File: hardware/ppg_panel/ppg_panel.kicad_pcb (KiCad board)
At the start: 2 copper layers, 70 x 110 mm, 68 parts

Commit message: Convert PPG passives to SMD and refresh compact V-cut panel
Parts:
- OPT_C1, OPT_C2: footprint OPT_PPG:Bypass_100n_P2.5mm -> OPT_PPG:C0805_Hand
- TX_R4, TX_R9: footprint TX_TX:R -> TX_TX:RSense
- moved TX_R1 3.81 mm to (62.8, 132.0)
- moved TX_R2 3.81 mm to (62.8, 136.0)
- moved TX_R3 3.81 mm to (73.0, 138.3)
- moved TX_R4 3.81 mm to (65.8, 151.0)
- moved TX_R6 3.81 mm to (99.8, 132.0)
- moved TX_R7 3.81 mm to (99.8, 136.0)
- moved TX_R8 3.81 mm to (99.8, 140.0)
- moved TX_R9 3.81 mm to (101.8, 151.0)
- moved TX_H3 2.00 mm to (54.0, 154.0)
- moved TX_H4 2.00 mm to (116.0, 154.0)
- moved OPT_C1 1.25 mm to (63.2, 57.0)
- moved OPT_C2 1.25 mm to (101.7, 57.0)
- moved TX_C2 1.25 mm to (77.0, 144.2)
- moved TX_C4 1.25 mm to (93.0, 144.2)
- moved TX_C5 1.25 mm to (90.1, 131.0)
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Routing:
- net TX/GND: track 0.00 -> 11.6 mm, vias 0 -> 6
- net TX/CMD_RED: track 29.6 -> 35.2 mm, vias 0 -> 1
- net TX/CMD_IR: track 21.7 -> 27.3 mm, vias 0 -> 2
- net TX/AMP_RED: track 14.3 -> 17.3 mm
- net TX/AMP_IR: track 21.2 -> 24.2 mm, vias 0 -> 1
- net TX/DAC_IR: track 41.5 -> 44.3 mm, vias 0 -> 1
- net TX/DAC_RED: track 46.7 -> 49.5 mm, vias 0 -> 1
- net TX/BASE_RED: track 10.1 -> 12.9 mm
- net TX/BASE_IR: track 6.34 -> 9.15 mm
- net TX/SENSE_RED: track 35.8 -> 38.3 mm, vias 0 -> 2
- net TX/SENSE_IR: track 46.2 -> 48.6 mm, vias 0 -> 2
- net TX/5V: track 68.4 -> 69.8 mm, vias 0 -> 1
- net OPT/3V3_RED: track 38.1 -> 38.3 mm, vias 0 -> 1
- net OPT/3V3_IR: track 43.8 -> 44.0 mm, vias 0 -> 1
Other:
- board size 70 x 110 mm -> 70 x 108 mm
- board text added: "PPG RX v1.4"
- board text added: "PPG TX v1.8"
- board text removed: "5V GND"
- board text removed: "DAC: 3.3V ONLY"
- board text removed: "IR A+ K-"
- board text removed: "J2 PI: SCL SDA 3V3 GND"
- board text removed: "PPG RX v1.3"
- board text removed: "PPG TX v1.7"
- board text removed: "RED A+ K-"

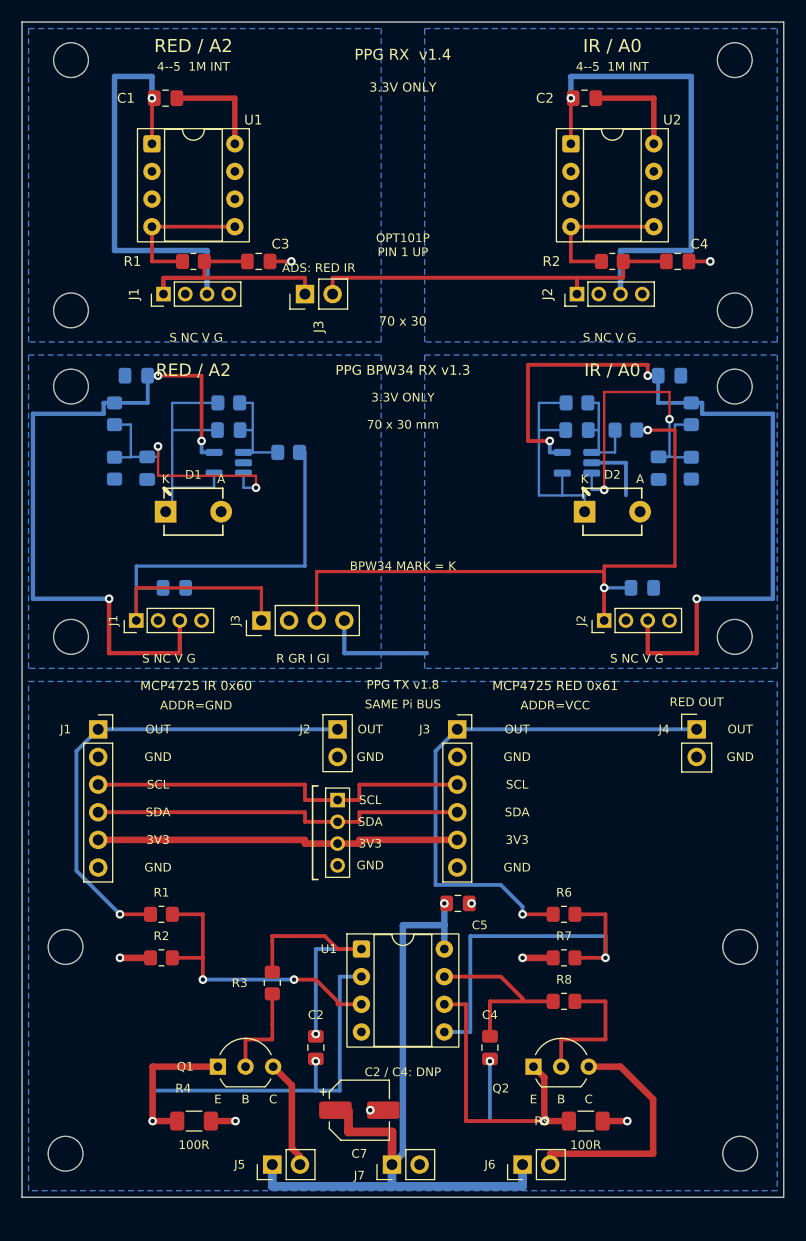
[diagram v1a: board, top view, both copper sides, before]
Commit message: Shrink PPG receivers to 70x20 and driver to 70x40; refresh V-cut release
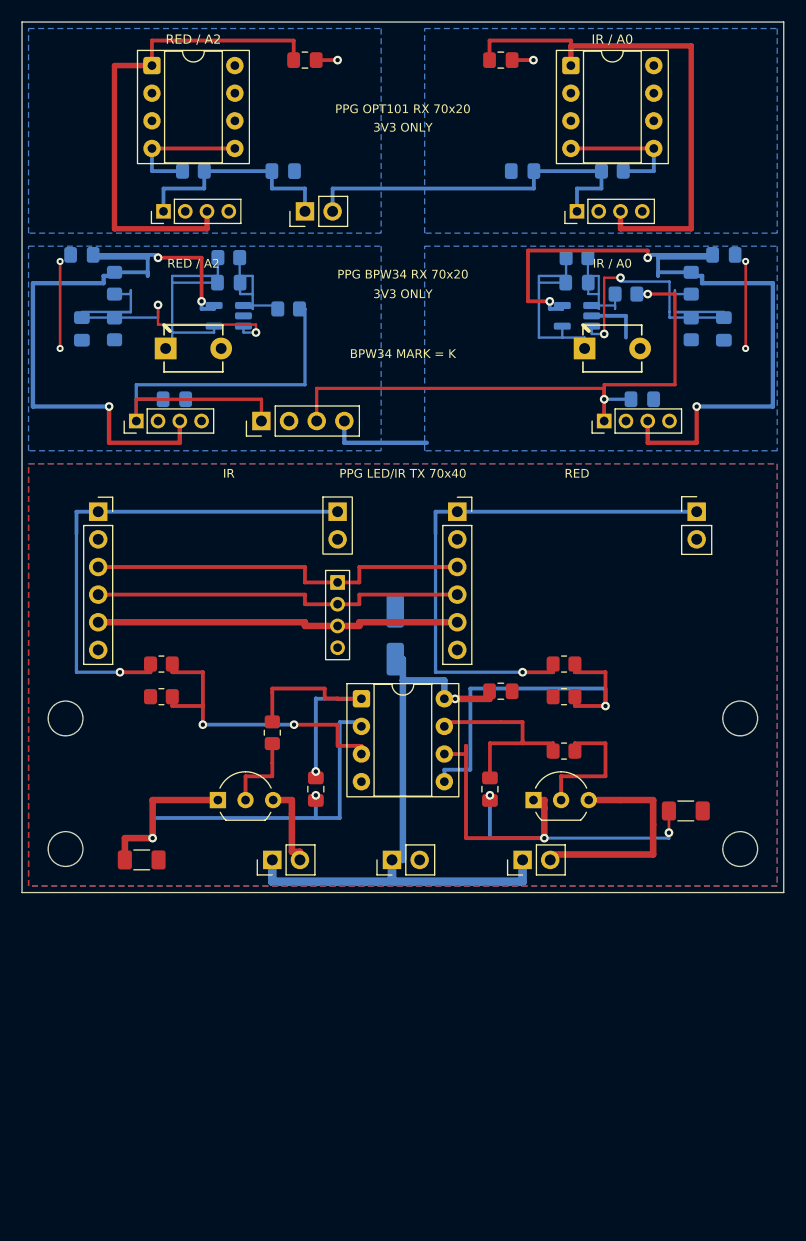
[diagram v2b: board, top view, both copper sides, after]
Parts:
- removed BPW_H1, BPW_H2, BPW_H3, BPW_H4: M3 / 3.2mm NPTH, BPW_PPG:MountingHole_M3
- removed OPT_H1, OPT_H2, OPT_H3, OPT_H4: M3 / 3.2mm NPTH, OPT_PPG:MountingHole_M3
- OPT_C3, OPT_C4, OPT_R1, OPT_R2, TX_C7: moved to B.Cu
- moved TX_C7 43.8 mm to (84.3, 106.3), turned to 90 degrees
- moved TX_R9 29.9 mm to (111.0, 122.5)
- moved TX_H3 28.0 mm to (54.0, 126.0)
- moved TX_H4 28.0 mm to (116.0, 126.0)
- moved TX_J5 28.0 mm to (73.0, 127.0)
- moved TX_J6 28.0 mm to (96.0, 127.0)
- moved TX_J7 28.0 mm to (84.0, 127.0)
- moved TX_Q1 24.5 mm to (68.0, 121.5)
- moved TX_Q2 24.5 mm to (97.0, 121.5)
- moved TX_R4 24.5 mm to (61.0, 127.0)
- moved TX_R2 24.0 mm to (62.8, 112.0)
- moved TX_R7 24.0 mm to (99.8, 112.0)
- moved TX_C2 23.8 mm to (77.0, 120.5)
- moved TX_C4 23.8 mm to (93.0, 120.5)
- moved TX_R1 23.0 mm to (62.8, 109.0)
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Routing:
- net TX/GND: track 11.6 -> 0.00 mm, vias 6 -> 0
- net TX/5V: track 69.8 -> 59.5 mm
- net OPT/GND_RED: track 11.5 -> 1.96 mm
- net OPT/GND_IR: track 11.5 -> 1.96 mm
- net BPW/OUT_IR: track 65.4 -> 56.5 mm
- net BPW/GND_RED: track 0.00 -> 8.00 mm, vias 0 -> 2
- net TX/SENSE_RED: track 38.3 -> 46.3 mm, vias 2 -> 3
- net BPW/VREF_RED: track 24.8 -> 32.3 mm
- net OPT/3V3_RED: track 38.3 -> 45.7 mm, vias 1 -> 0
- net BPW/OUT_RED: track 51.4 -> 44.3 mm
- net OPT/OUT_RED: track 26.7 -> 20.4 mm
- net BPW/GND_IR: track 16.7 -> 22.7 mm, vias 0 -> 2
- net OPT/3V3_IR: track 44.0 -> 49.3 mm, vias 1 -> 0
- net BPW/SUM_RED: track 25.0 -> 22.3 mm
- net BPW/SUM_IR: track 21.2 -> 18.6 mm
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- added copper zone on F.Cu, net TX/GND
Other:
- board size 70 x 108 mm -> 70 x 80 mm
- board text added: "3V3 ONLY"
- board text added: "IR"
- board text added: "IR-"
- board text added: "PPG BPW34 RX 70x20"
- board text added: "PPG LED/IR TX 70x40"
- board text added: "PPG OPT101 RX 70x20"
- board text added: "RED"
- board text added: "RED-"
- board text added: "S"
- board text removed: "100R"
- board text removed: "3.3V ONLY"
- board text removed: "4--5 1M INT"
- board text removed: "70 x 30"
- board text removed: "70 x 30 mm"
- board text removed: "A+"
- board text removed: "ADDR=GND"
- board text removed: "ADDR=VCC"
- board text removed: "ADS: RED IR"
- board text removed: "C1"
- board text removed: "C2"
- board text removed: "C2 / C4: DNP"
- board text removed: "C3"
- board text removed: "C4"
- board text removed: "C5"
- board text removed: "C6"
- board text removed: "C7"
- board text removed: "C8"
- board text removed: "D1"
- board text removed: "D1 RED"
- board text removed: "D2"
- board text removed: "D2 IR"
- board text removed: "GR/GI=CHANNEL GND"
- board text removed: "IR_OUT"
- board text removed: "J1"
- board text removed: "J1 A2 RED"
- board text removed: "J1 IR DAC"
- board text removed: "J2"
- board text removed: "J2 A0 IR"
- board text removed: "J2 PI"
- board text removed: "J3"
- board text removed: "J3 ADS"
- board text removed: "J3 RED DAC"
- board text removed: "J4"
- board text removed: "J4 RED OUT"
- board text removed: "J5"
- board text removed: "J5 IR LED"
- board text removed: "J6"
- board text removed: "J6 RED LED"
- board text removed: "J7"
- board text removed: "J7 POWER"
- board text removed: "K-"
- board text removed: "MCP4725 IR 0x60"
- board text removed: "MCP4725 RED 0x61"
- board text removed: "N"
- board text removed: "OPT101P PIN 1 UP"
- board text removed: "PPG BPW34 RX v1.3"
- board text removed: "PPG RX v1.4"
- board text removed: "PPG TX v1.8"
- board text removed: "Q1"
- board text removed: "Q1 IR E-B-C"
- board text removed: "Q2"
- board text removed: "Q2 RED E-B-C"
- board text removed: "R GR I GI"
- board text removed: "R1"
- board text removed: "R2"
- board text removed: "R3"
- board text removed: "R4"
- board text removed: "R5"
- board text removed: "R6"
- board text removed: "R7"
- board text removed: "R8"
- board text removed: "R9"
- board text removed: "R=OUT_RED I=OUT_IR"
- board text removed: "RED OUT"
- board text removed: "RED_OUT"
- board text removed: "S NC V G"
- board text removed: "SAME Pi BUS"
- board text removed: "U1"
- board text removed: "U1 LM358"
- board text removed: "U1 RED OPT101"
- board text removed: "U2"
- board text removed: "U2 IR OPT101"
- board text removed: "V=3V3 GR/GI=GND"
- board text removed: "V=3V3 N=NC"

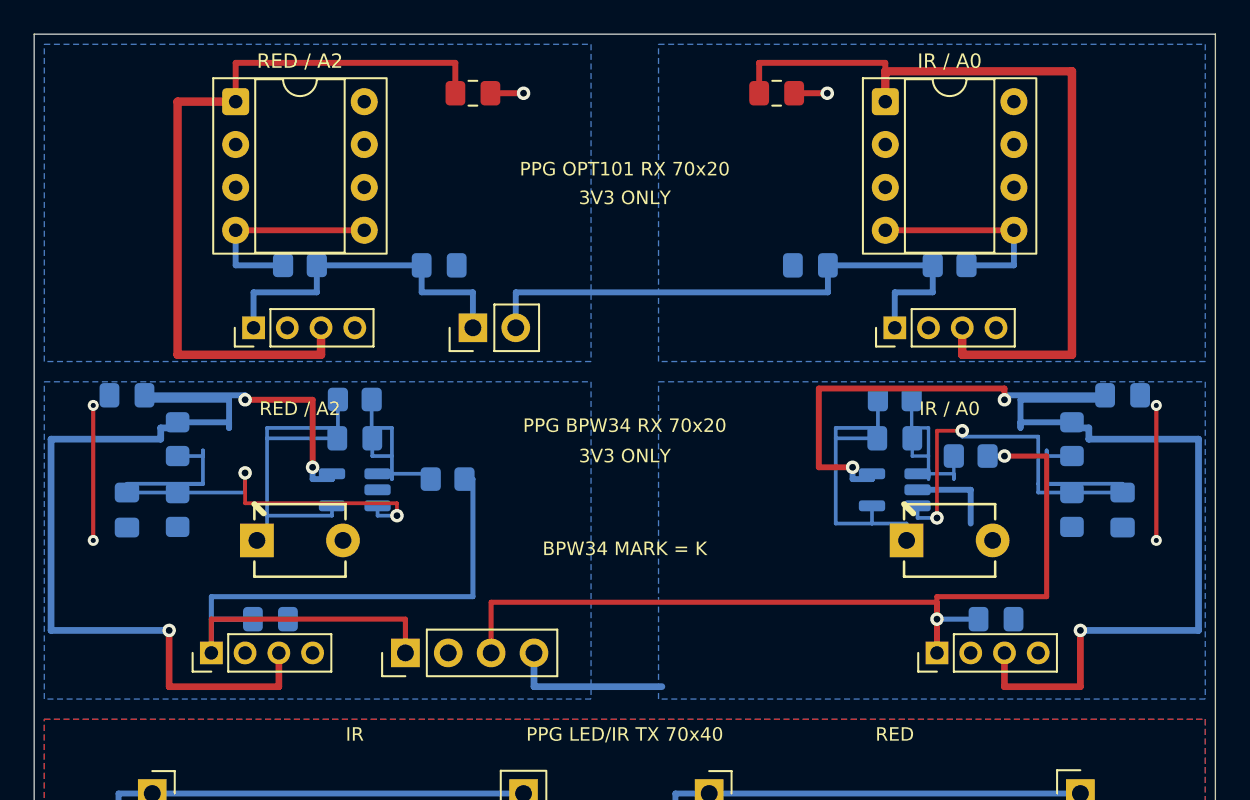
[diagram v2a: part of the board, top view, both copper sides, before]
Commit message: Increase V-score copper and component margins; reposition receiver circuits
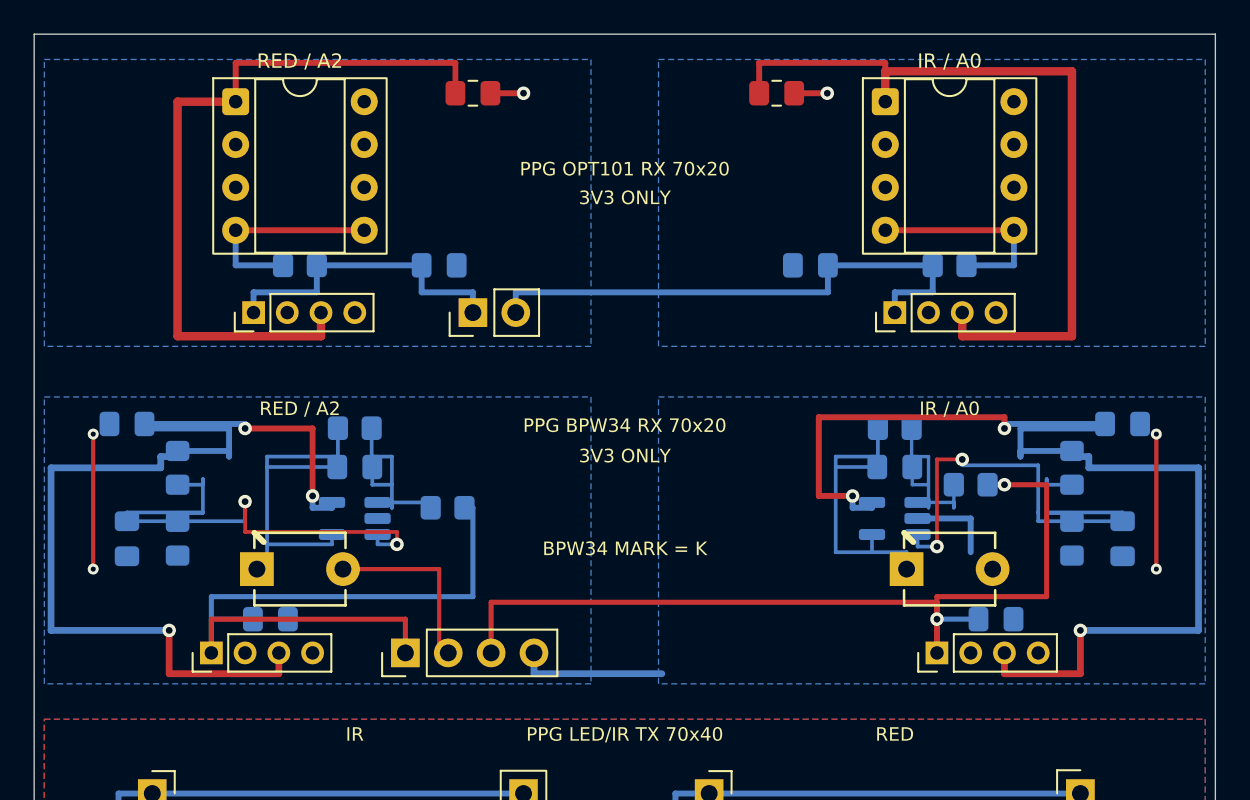
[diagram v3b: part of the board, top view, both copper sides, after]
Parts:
- moved BPW_C1 1.70 mm to (69.0, 75.7)
- moved BPW_C2 1.70 mm to (101.0, 75.7)
- moved BPW_C3 1.70 mm to (55.5, 79.9)
- moved BPW_C4 1.70 mm to (114.5, 79.9)
- moved BPW_D1 1.70 mm to (65.8, 81.7)
- moved BPW_D2 1.70 mm to (104.2, 81.7)
- moved BPW_R3 1.70 mm to (74.5, 78.1)
- moved BPW_R4 1.70 mm to (105.5, 76.7)
- moved BPW_R5 1.70 mm to (58.5, 75.7)
- moved BPW_R6 1.70 mm to (111.5, 75.7)
- moved BPW_R7 1.70 mm to (58.5, 79.9)
- moved BPW_R8 1.70 mm to (111.5, 79.9)
- moved BPW_U1 1.70 mm to (69.0, 78.7)
- moved BPW_U2 1.70 mm to (101.0, 78.7)
- moved BPW_C5 1.70 mm to (55.5, 73.1)
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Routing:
- net BPW/GND_RED: track 8.00 -> 19.2 mm
- net BPW/3V3_IR: track 73.7 -> 70.5 mm
- net BPW/3V3_RED: track 65.4 -> 62.2 mm
- net OPT/OUT_RED: track 20.4 -> 18.6 mm
- net OPT/OUT_IR: track 34.4 -> 32.6 mm
- net BPW/OUT_RED: track 44.3 -> 42.6 mm
- net BPW/OUT_IR: track 56.5 -> 54.8 mm
- net OPT/3V3_RED: track 45.7 -> 44.4 mm
- net OPT/3V3_IR: track 49.3 -> 48.0 mm
- net BPW/GND_IR: track 22.7 -> 22.0 mm

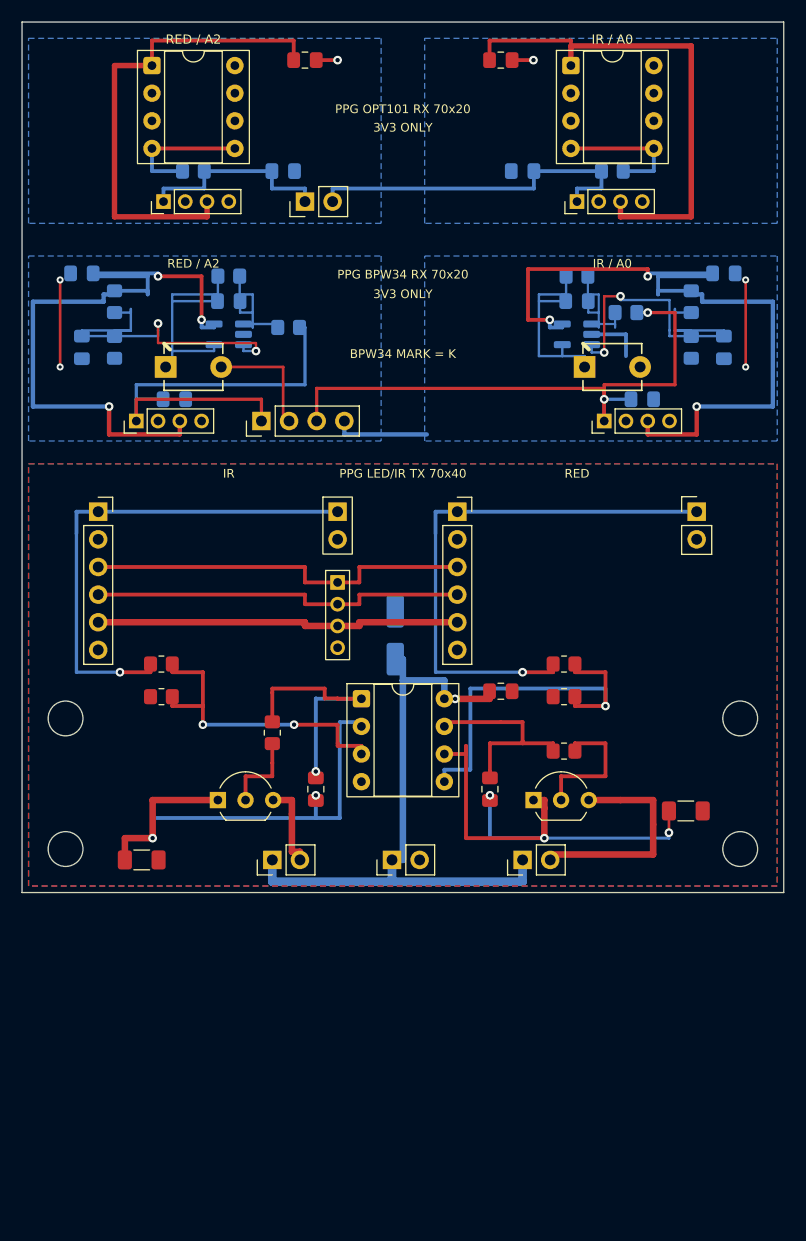
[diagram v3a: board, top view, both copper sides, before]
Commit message: Chamfer PPG board routing to 45 degrees and verify V-score fabrication release
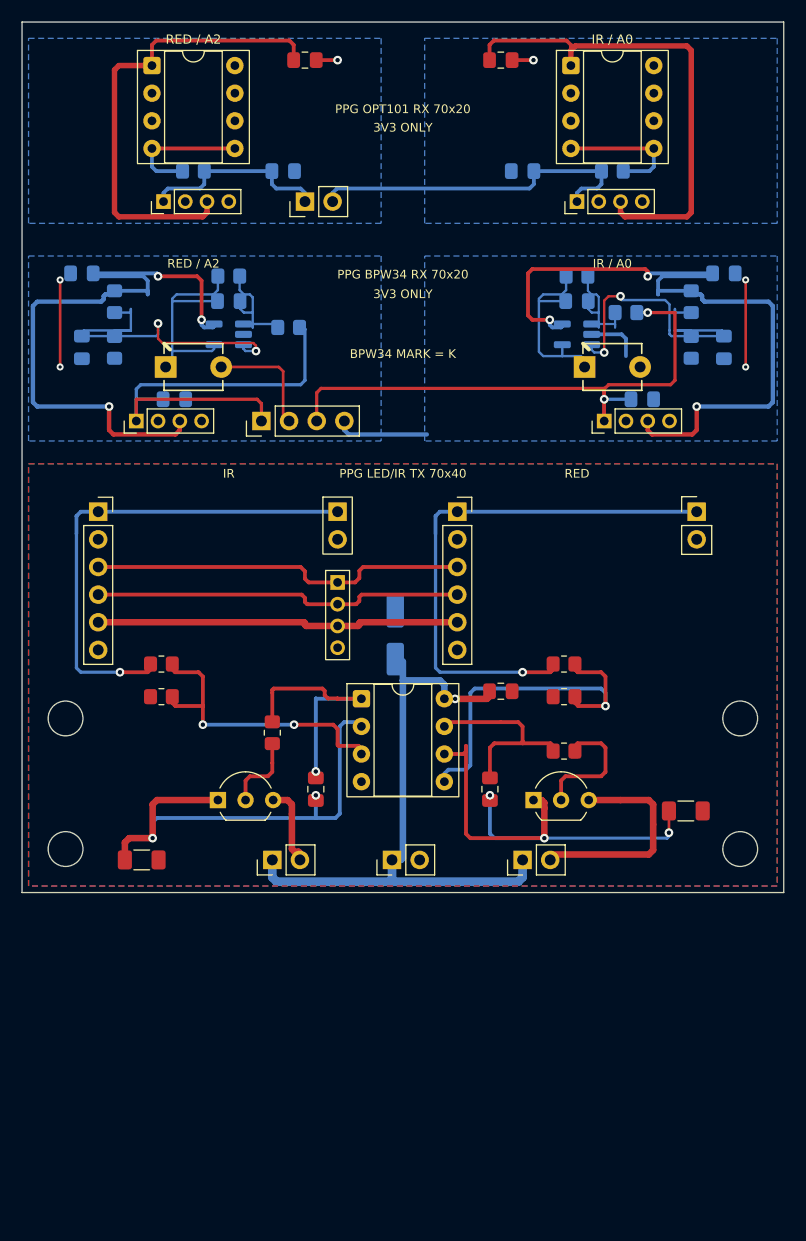
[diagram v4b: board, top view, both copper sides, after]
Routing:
- net BPW/3V3_IR: track 70.5 -> 68.1 mm
- net BPW/3V3_RED: track 62.2 -> 60.2 mm
- net TX/CMD_RED: track 35.3 -> 33.8 mm
- net OPT/3V3_IR: track 48.0 -> 46.6 mm
- net OPT/3V3_RED: track 44.4 -> 43.2 mm
- net TX/SENSE_IR: track 46.5 -> 45.3 mm
- net TX/5V: track 59.5 -> 58.4 mm
- net TX/CMD_IR: track 29.3 -> 28.3 mm
- net OPT/OUT_RED: track 18.6 -> 17.7 mm
- net OPT/OUT_IR: track 32.6 -> 31.6 mm
- net BPW/SUM_IR: track 18.6 -> 17.7 mm
- net BPW/VREF_IR: track 32.6 -> 31.7 mm
- net TX/SCL: track 35.8 -> 35.0 mm
- net TX/SENSE_RED: track 46.3 -> 45.4 mm
- net TX/BASE_RED: track 12.8 -> 12.0 mm
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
